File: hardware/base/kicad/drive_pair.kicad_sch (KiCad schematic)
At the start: 30 parts, among them J6 DRIVE, J7 DRIVE, Q1 AO3422, Q2 AO3422, U11 ST26C31BDR, U12 LTV-357T-C, U13 TPD4E05U06DQAR, U14 LTV-357T-C, U15 TPD4E05U06DQAR

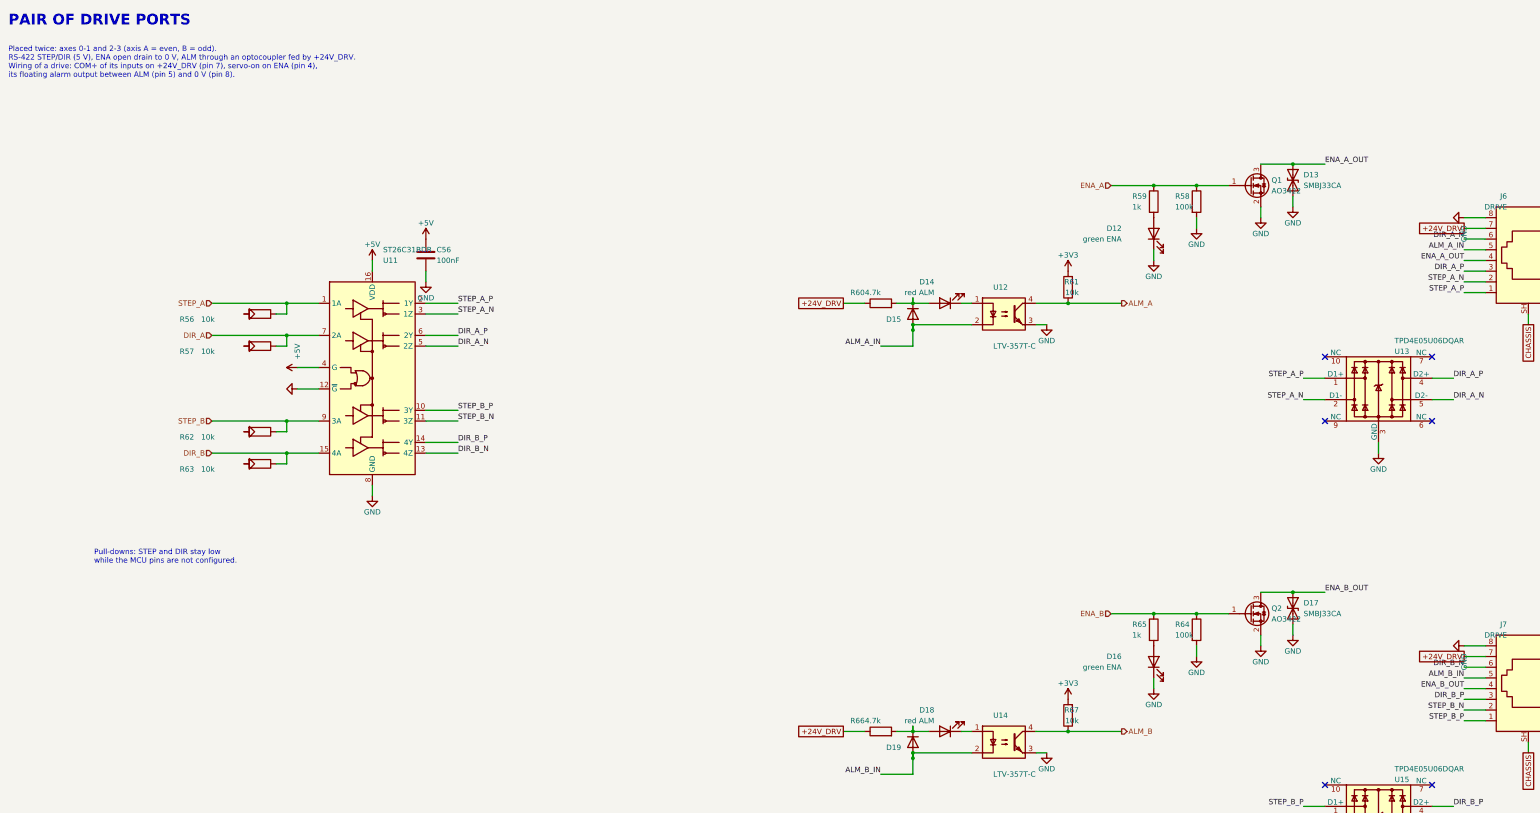
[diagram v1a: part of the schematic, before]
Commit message: Accept a 12 V or 24 V supply on the base board (10.8 to 30 V)
- Supply nets renamed +VIN and +VIN_OUT (silkscreen VIN OUT).
- UVLO 200 k over 47 k // 100 k: start 8.47 V (9.48 V worst case),
  stop 7.79 V; fuse 3.5 A (12H1350C).
- 0-10 V: OPA2990 rail-to-rail op amp supplied by +VIN, SS8550 current
  limit across the 120 ohm; 10 V into 10 k from 10.9 V of supply.
- E-stop and probe inputs: 2 x 4.7 k in parallel, shunts 1 k and 4.7 k.
- Buck simulated from 7.8 to 30 V with the smallest slope compensation
  the datasheet allows: 79 deg, 11.6 dB minimum.
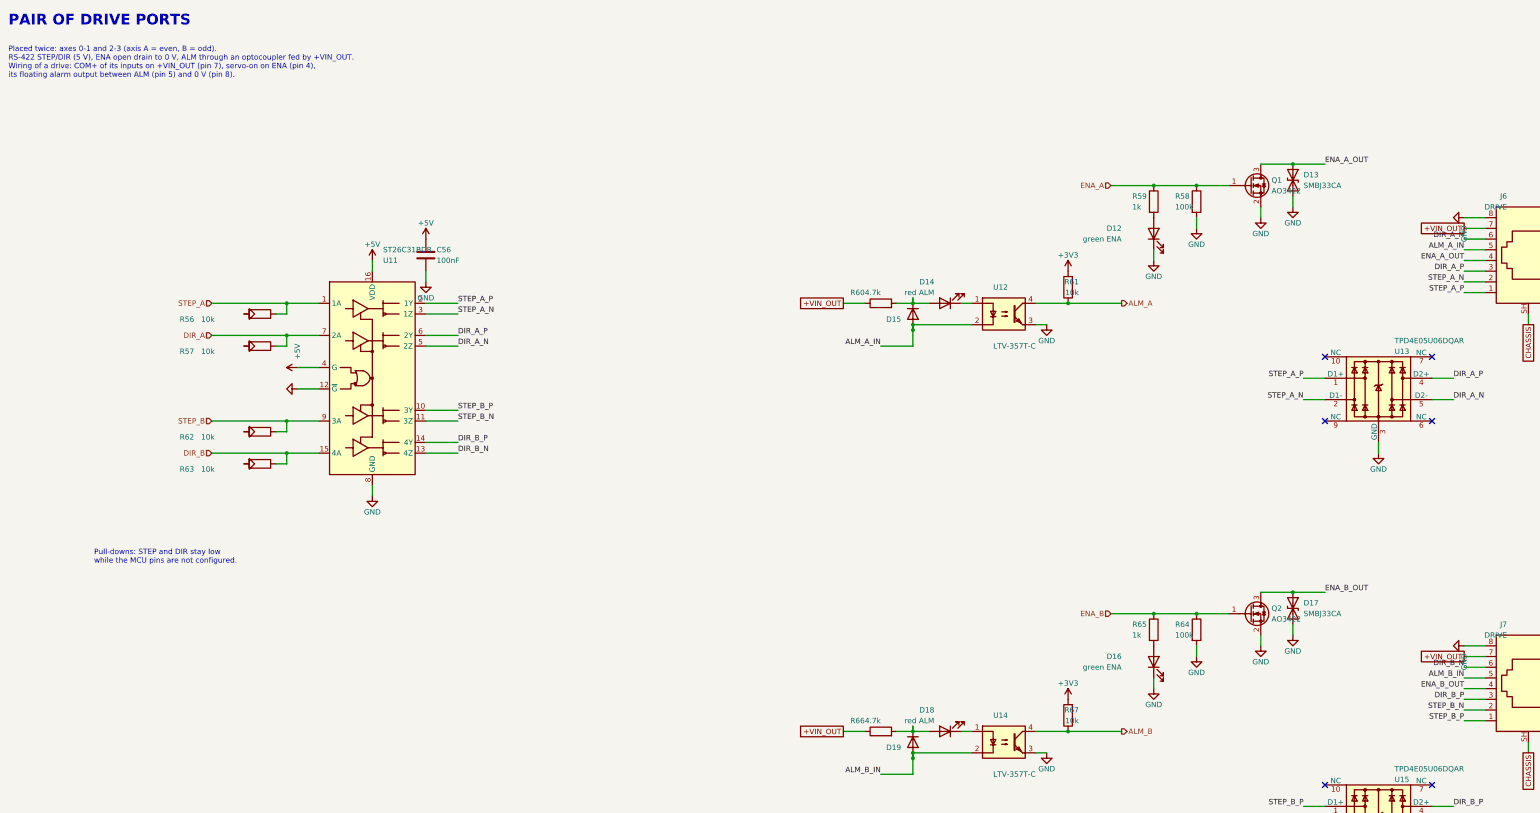
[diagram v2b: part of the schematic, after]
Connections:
- net +24V_DRV renamed +VIN_OUT
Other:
- note added: "Placed twice: axes 0-1 and 2-3 (axis A = even, B = odd). RS-422 STEP/DIR (5 V), ENA open drain to 0 V, ALM through an optocoupler fed by +VIN_OUT. Wiring of a drive: COM+ of its inputs on +VIN_OUT (pin 7), servo-on on ENA (pin 4), its floating alarm output between ALM (pin 5) and 0 V (pin 8)."
- note removed: "Placed twice: axes 0-1 and 2-3 (axis A = even, B = odd). RS-422 STEP/DIR (5 V), ENA open drain to 0 V, ALM through an optocoupler fed by +24V_DRV. Wiring of a drive: COM+ of its inputs on +24V_DRV (pin 7), servo-on on ENA (pin 4), its floating alarm output between ALM (pin 5) and 0 V (pin 8)."

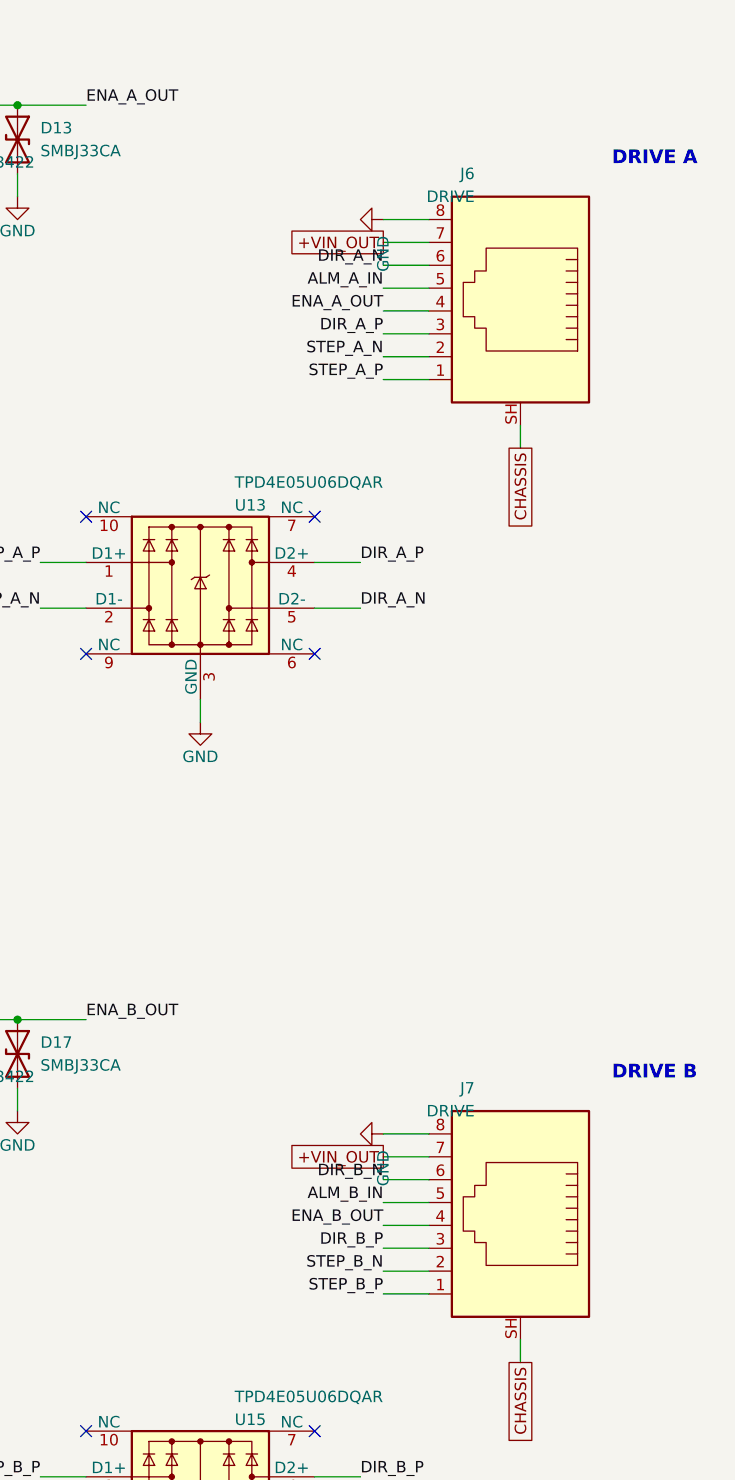
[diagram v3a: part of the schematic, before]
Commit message: Start the base board PCB: outline, profile rules, connectors on the edges
- pcb.py builds the board from the schematic: 72 x 150 mm, 4 layers,
  C-LOCK keyhole, M3 holes, connectors on both long edges; the other
  parts are parked beside the board until they are placed.
- base.kicad_dru: rules of the Phoenix UM-BASIC 72 profile (no part at
  the short edges on the top side, no through-hole lead on the rim the
  board rests on), proved by the DRC.
- Dual shielded RJ45 per axis (HC-WK88-H132-1X2-55B): port A for the
  drive, port B for the encoder. kicadgen draws multi-unit symbols, one
  unit per sheet; footprint and 3D model generated from the datasheet.
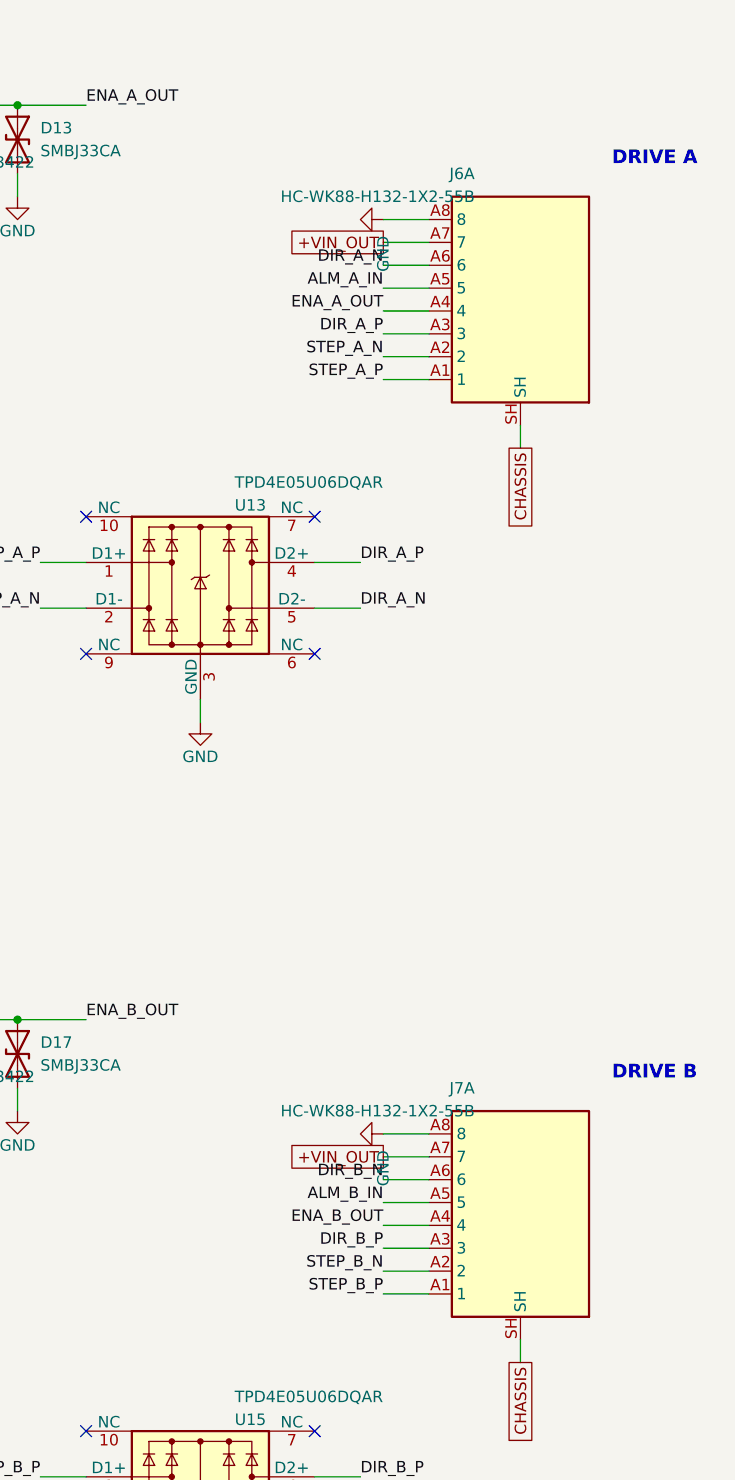
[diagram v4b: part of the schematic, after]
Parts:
- J6, J7: value DRIVE -> HC-WK88-H132-1X2-55B; footprint Bornier:RJ45_HOAUC_HYCW48-RJ45-163B -> Bornier:RJ45x2_HongCheng_HC-WK88-H132-1X2-55B; symbol Connector:RJ45_Shielded -> Bornier:RJ45x2_Shielded; LCSC C3001539 -> C7501828
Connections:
- net +VIN_OUT: now also J6.A7 (7), J7.A7 (7); no longer J6.7, J7.7
- net ALM_A_IN: now also J6.A5 (5); no longer J6.5
- net ALM_B_IN: now also J7.A5 (5); no longer J7.5
- net DIR_A_N: now also J6.A6 (6); no longer J6.6
- net DIR_A_P: now also J6.A3 (3); no longer J6.3
- net DIR_B_N: now also J7.A6 (6); no longer J7.6
- net DIR_B_P: now also J7.A3 (3); no longer J7.3
- net ENA_A_OUT: now also J6.A4 (4); no longer J6.4
- net ENA_B_OUT: now also J7.A4 (4); no longer J7.4
- net GND: now also J6.A8 (8), J7.A8 (8); no longer J6.8, J7.8
- net STEP_A_N: now also J6.A2 (2); no longer J6.2
- net STEP_A_P: now also J6.A1 (1); no longer J6.1
- net STEP_B_N: now also J7.A2 (2); no longer J7.2
- net STEP_B_P: now also J7.A1 (1); no longer J7.1
